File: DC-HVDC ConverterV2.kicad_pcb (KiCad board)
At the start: 2 copper layers, 28 parts, among them J1 Schraubklemme, J2 Conn_01x02_Pin, J3 4er Pinreihe, J4 5er Buchsenleiste, Q1 IRF740, U3 TL3843P, U4 SKM10A-12

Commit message: ab hier mit neuem DC-DC Isolator
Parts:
- removed U4: SKM10A-12, footprints:SKM10A_MWU
- added U1: ~, Eigene:DKB3-12S2PH3, F.Cu at (165.5, 113.8)
- R7: footprint Resistor_SMD:R_2512_6332Metric -> Resistor_THT:R_Bare_Metal_Element_L12.4mm_W4.8mm_P11.40mm
- moved C2 7.18 mm to (163.4, 106.0), turned to 90 degrees
- moved R7 4.16 mm to (119.5, 101.2)
- moved C3 0.90 mm to (114.0, 115.1)
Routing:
- net +12V: track 58.7 -> 52.4 mm
- net Net-(Q1-S): track 22.5 -> 20.8 mm
- net /HVDC2: track 40.1 -> 38.5 mm
- net +12V_FLOATING: track 42.3 -> 40.9 mm
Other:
- board text added: "FLOATING SIDE"
- board text added: "GROUNDED SIDE"

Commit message: Fehler im PCB Layout ausgebessert
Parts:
- C1: footprint Capacitor_THT:CP_Radial_D12.5mm_P7.50mm -> Capacitor_THT:CP_Radial_D13.0mm_P5.00mm
- C3: footprint Capacitor_THT:CP_Radial_D14.0mm_P7.50mm -> Capacitor_THT:CP_Radial_D7.5mm_P2.50mm
- R3: footprint Resistor_THT:R_Axial_DIN0204_L3.6mm_D1.6mm_P7.62mm_Horizontal -> Resistor_THT:R_Axial_DIN0207_L6.3mm_D2.5mm_P10.16mm_Horizontal
- R7: footprint Resistor_THT:R_Bare_Metal_Element_L12.4mm_W4.8mm_P11.40mm -> Resistor_THT:R_Bare_Metal_Element_L16.3mm_W4.8mm_P15.30mm
- moved C2 8.10 mm to (163.4, 114.1), turned to -90 degrees
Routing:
- net +12V_FLOATING: track 40.9 -> 44.3 mm
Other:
- board text added: "! 200V !"
- board text removed: "!"
- board text removed: "HIGH VOLTAGE"

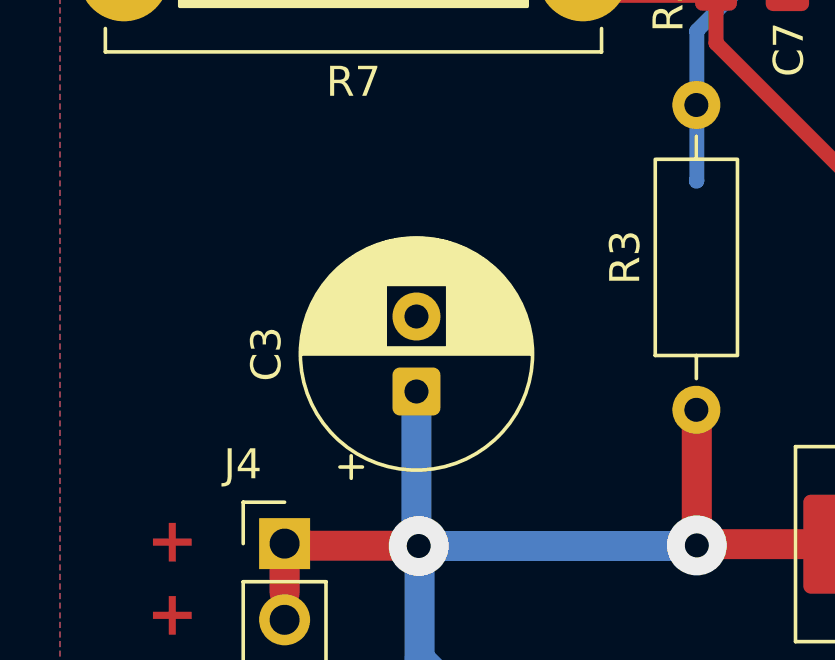
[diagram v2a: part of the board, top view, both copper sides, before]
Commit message: Änderungen nach PCB-V1
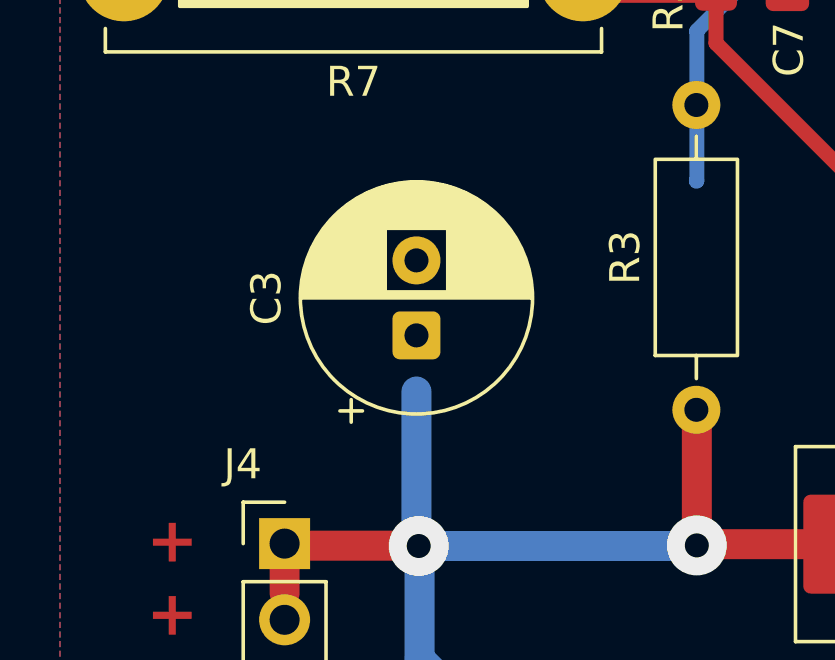
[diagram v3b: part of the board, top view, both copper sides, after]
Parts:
- moved C3 1.87 mm to (114.0, 113.2)
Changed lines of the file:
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@@
 	(footprint "Capacitor_THT:CP_Radial_D7.5mm_P2.50mm"
 		(layer "F.Cu")
-		(at 113.99 115.07 90)
+		(at 113.99 113.2 90)
 		(descr "CP, Radial series, Radial, pin pitch=2.50mm, diameter=7.5mm, height=8mm, Electrolytic Capacitor")
 		(tags "CP Radial series Radial pin pitch 2.50mm diameter 7.5mm height 8mm Electrolytic Capacitor")
